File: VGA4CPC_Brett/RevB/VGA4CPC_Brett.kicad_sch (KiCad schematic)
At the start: 45 parts, among them J1 +5V IN, J2 CPC PLUS AUDIO OUT, J3 CPC PLUS VIDEO IN, J4 CPC VIDEO IN, J5 VFREQ, J6 VGA OUT, J7 LUM OUT, SW1 RESET, U1 TLV3202AID, U2 TLV3202AID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

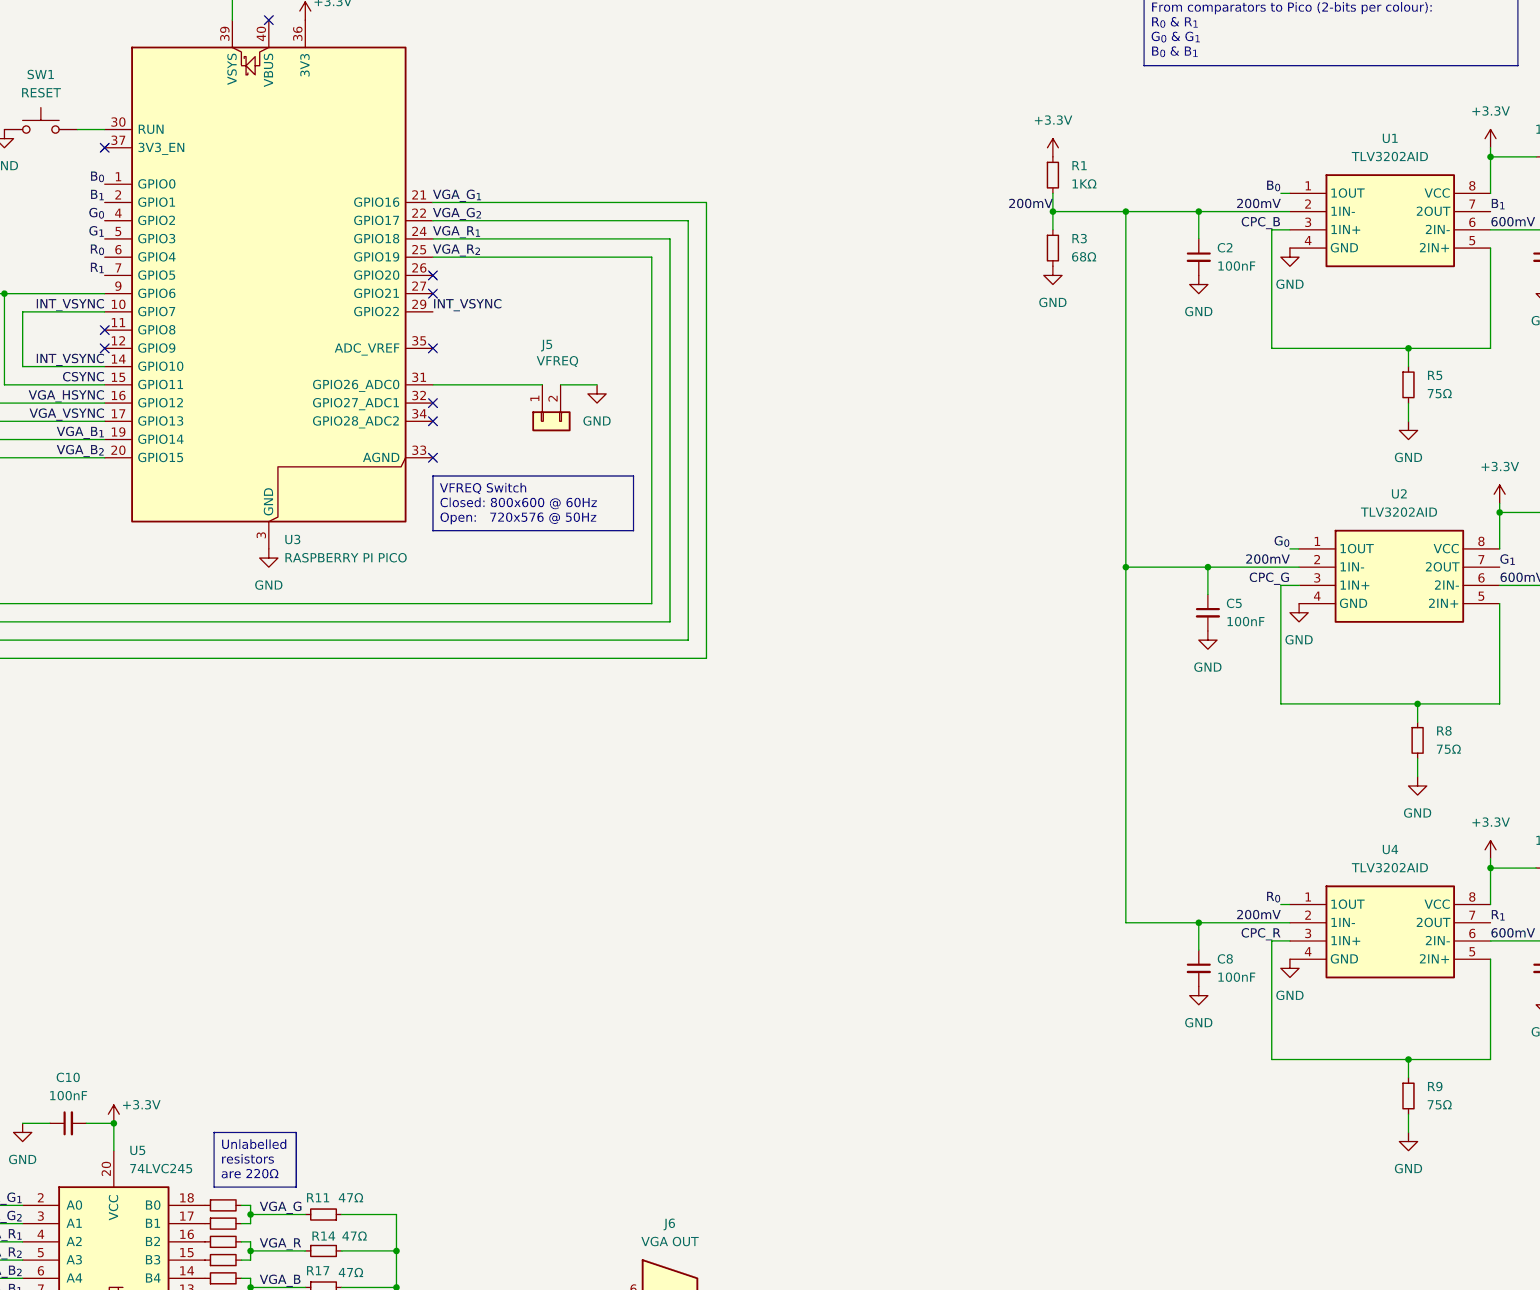
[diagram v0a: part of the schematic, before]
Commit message: Added BOM to schematic
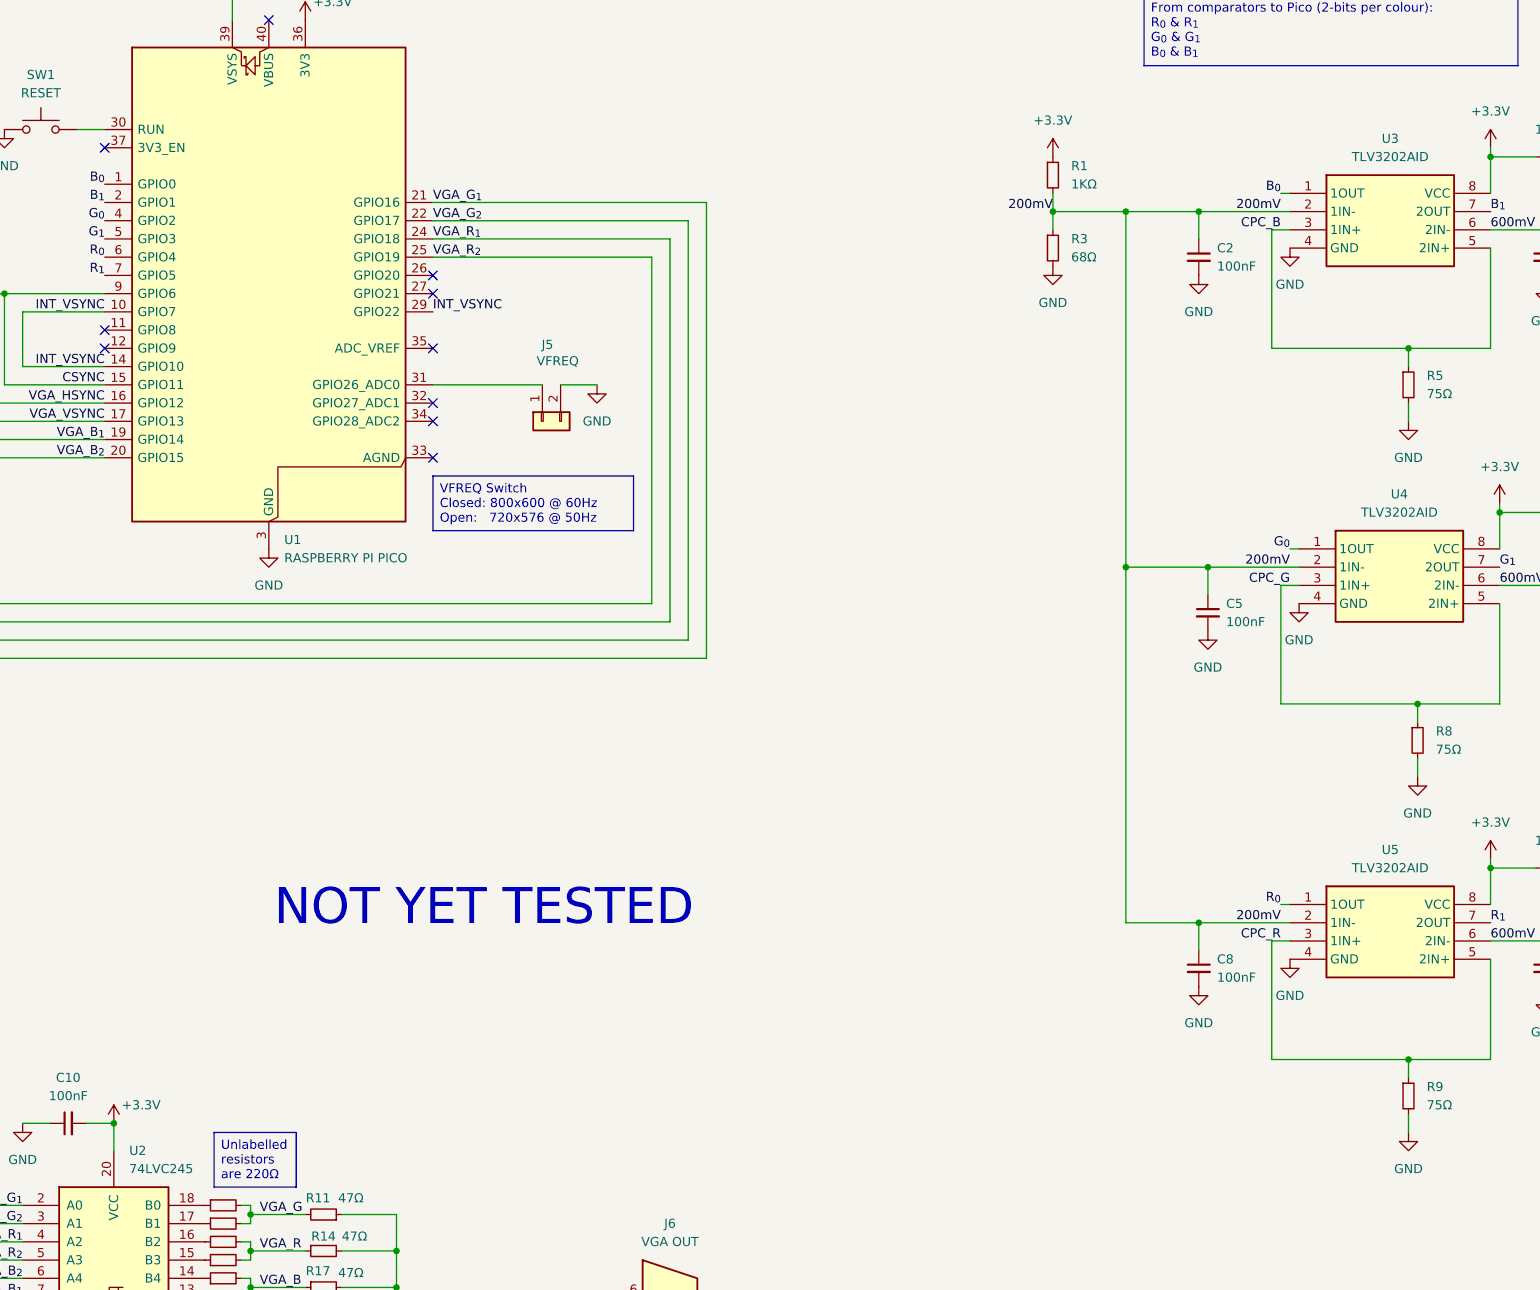
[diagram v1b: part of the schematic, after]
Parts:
- renumbered U3 to U1, U5 to U2, U1 to U3, U2 to U4, U4 to U5
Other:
- note added: "NOT YET TESTED"

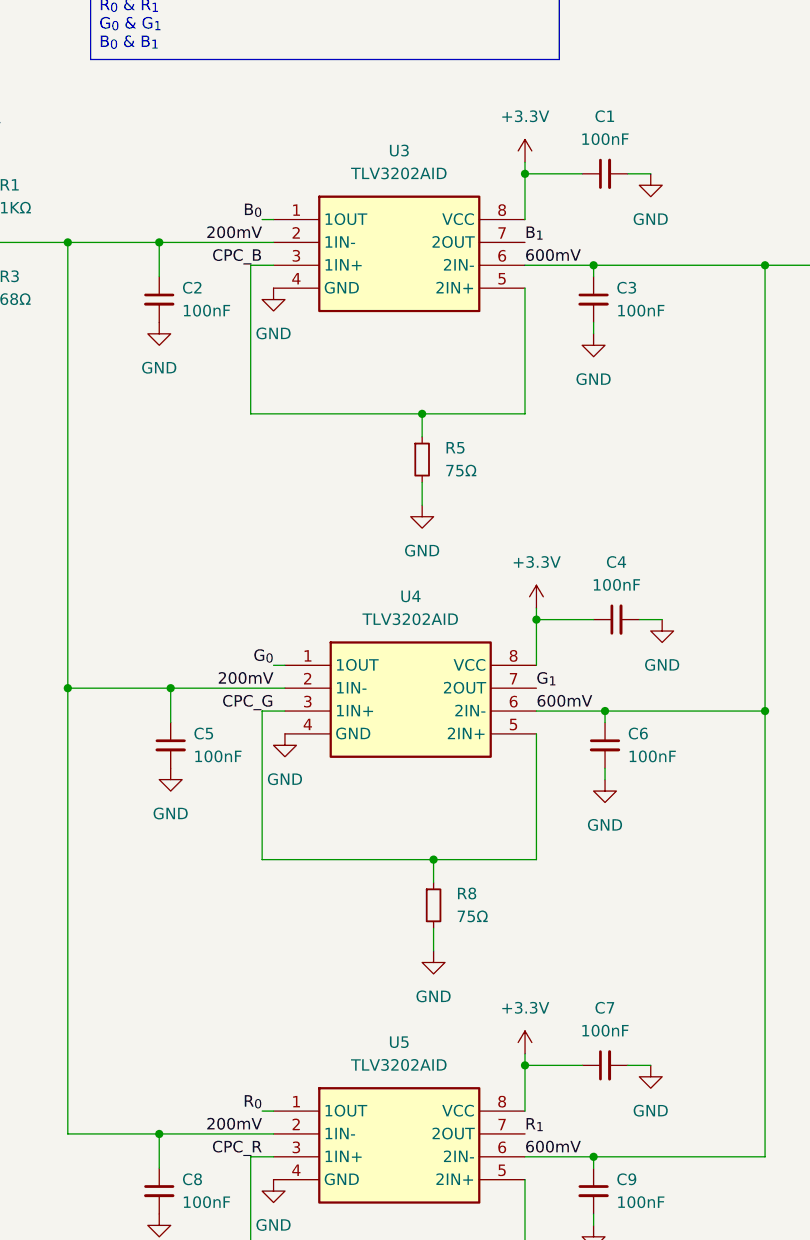
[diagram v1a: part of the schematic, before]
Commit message: Silkscreen updates
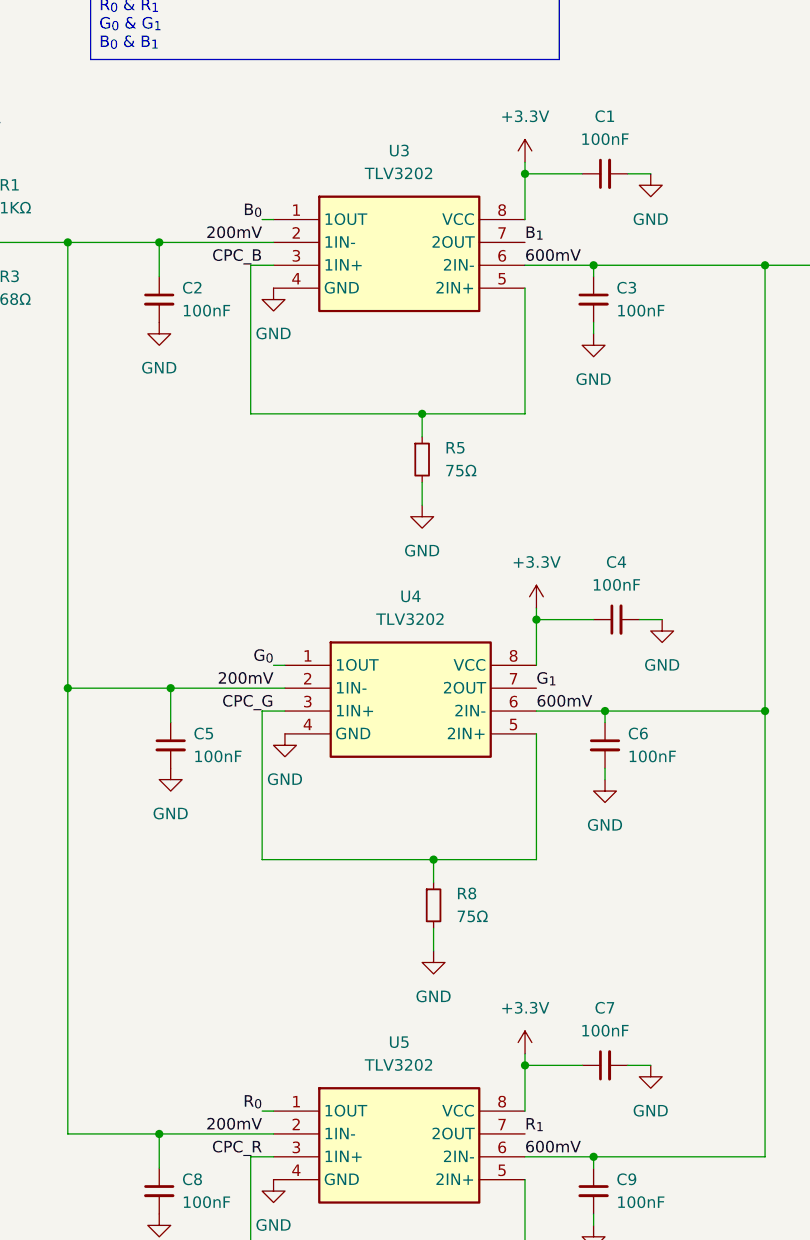
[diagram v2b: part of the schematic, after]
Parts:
- U3, U4, U5: value TLV3202AID -> TLV3202
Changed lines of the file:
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@@
 			)
 		)
-		(property "Value" "TLV3202AID"
+		(property "Value" "TLV3202"
 			(at 337.82 72.39 0)
 			(effects
@@
 			)
 		)
-		(property "Value" "TLV3202AID"
+		(property "Value" "TLV3202"
 			(at 337.82 171.45 0)
 			(effects
@@
 			)
 		)
-		(property "Value" "TLV3202AID"
+		(property "Value" "TLV3202"
 			(at 339.09 121.92 0)
 			(effects

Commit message: Spare GPIO ports routed
[1] Additional WACKED button (GPIO 21) for "future use"
[2] Spare GPIO 8/9/20 brought out to pin header for "future use"
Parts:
- added J8: SPARE GPIO, Connector_PinHeader_2.54mm:PinHeader_1x04_P2.54mm_Vertical, symbol Connector_Generic:Conn_01x04
- added SW2: WACKED, Button_Switch_THT:SW_PUSH_6mm, symbol Switch:SW_Push
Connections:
- net GND: now also J8.4 (Pin_4), SW2.2
- net GPIO8: now reaches U1.11 (GPIO8)
- net GPIO8: now also J8.1 (Pin_1)
- net GPIO9: now reaches U1.12 (GPIO9)
- net GPIO9: now also J8.2 (Pin_2)
- net GPIO20: now reaches U1.26 (GPIO20)
- net GPIO20: now also J8.3 (Pin_3)
- net at U1.27 (GPIO21): now also SW2.1
- no-connect marks 15 -> 11

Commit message: Broke out extra spare GPIO ports
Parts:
- removed J8: SPARE GPIO, Connector_PinHeader_2.54mm:PinHeader_1x04_P2.54mm_Vertical, symbol Connector_Generic:Conn_01x04
- added J8: SPARE GPIO, Connector_PinHeader_2.54mm:PinHeader_1x06_P2.54mm_Vertical, symbol Connector_Generic:Conn_01x06
- U3, U4, U5: value TLV3202 -> TLV3212
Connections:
- net GND: now also J8.6 (Pin_6)
- net GPIO20: now also J8.5 (Pin_5)
- net GPIO8: now also J8.3 (Pin_3)
- net GPIO9: now also J8.4 (Pin_4)
- net GPIO27: now reaches U1.32 (GPIO27_ADC1)
- net GPIO27: now also J8.2 (Pin_2)
- net GPIO28: now reaches U1.34 (GPIO28_ADC2)
- net GPIO28: now also J8.1 (Pin_1)
- no-connect marks 11 -> 9
